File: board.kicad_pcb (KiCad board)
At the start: 2 copper layers, 26.9 x 29 mm, 16 parts, among them J1 PMW3360, J2 MCU, U1 TLV70019_SOT23-5

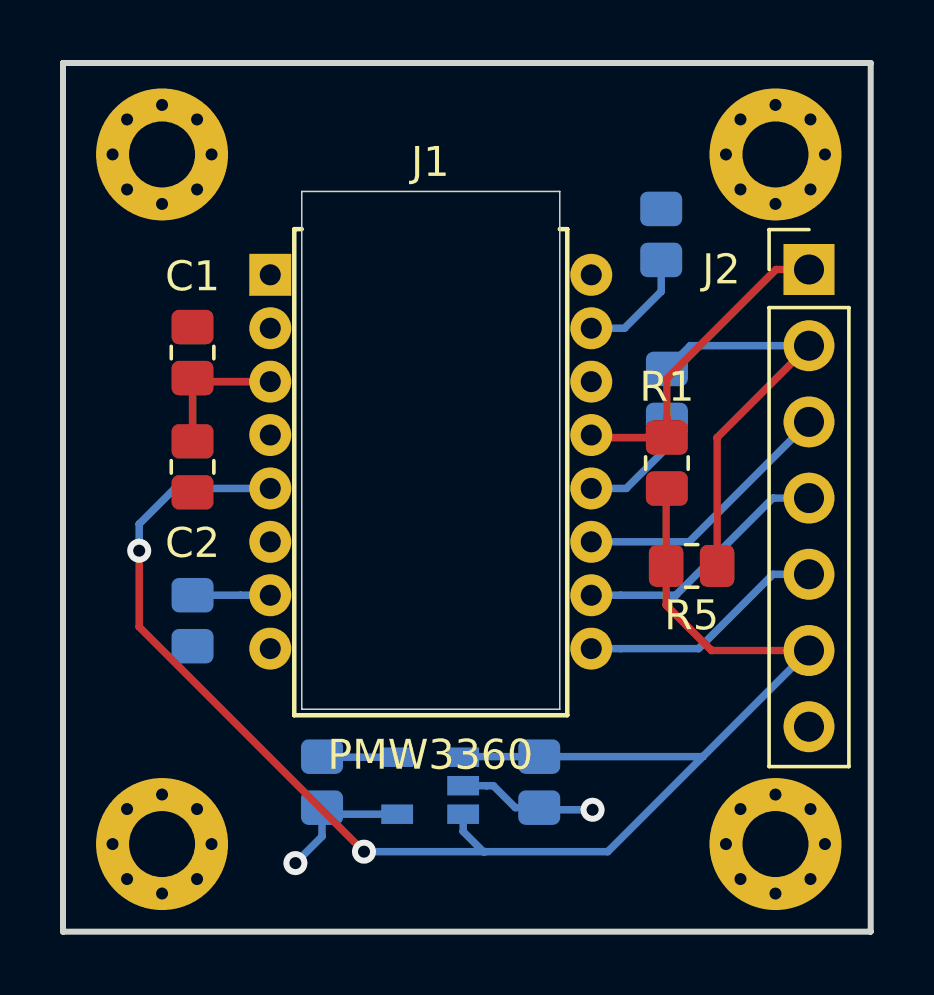
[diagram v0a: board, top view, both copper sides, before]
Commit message: Mounting holes
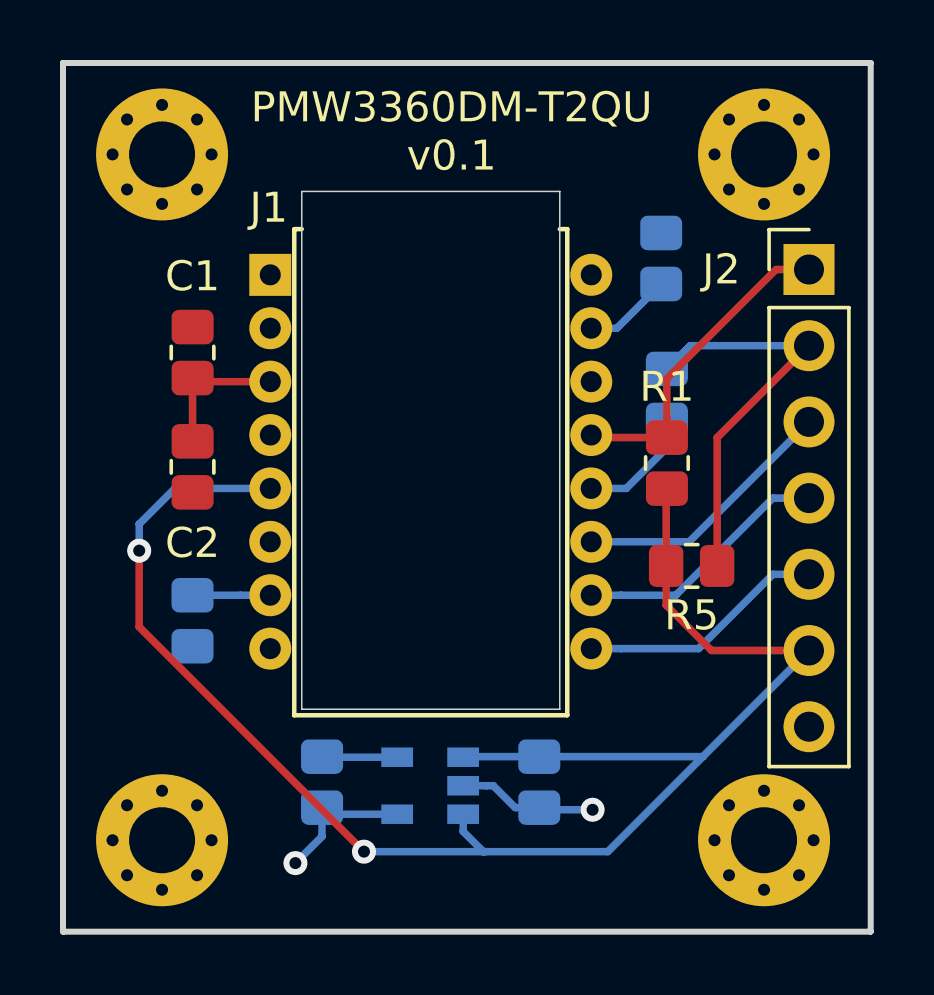
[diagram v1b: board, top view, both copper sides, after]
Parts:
- removed REF** (x4): MountingHole_2.2mm_M2_Pad_Via, MountingHole:MountingHole_2.2mm_M2_Pad_Via
- added J3: Mounting_Hole, MountingHole:MountingHole_2.2mm_M2_Pad_Via, F.Cu at (119.4, 72.4)
- added J4: Mounting_Hole, MountingHole:MountingHole_2.2mm_M2_Pad_Via, F.Cu at (119.4, 49.5)
- added J5: Mounting_Hole, MountingHole:MountingHole_2.2mm_M2_Pad_Via, F.Cu at (139.4, 72.4)
- added J6: Mounting_Hole, MountingHole:MountingHole_2.2mm_M2_Pad_Via, F.Cu at (139.4, 49.5)
- moved R2 0.80 mm to (136.0, 53.0)
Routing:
- net /LED_P: track 3.89 -> 2.94 mm
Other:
- board text added: "PMW3360DM-T2QU v0.1"

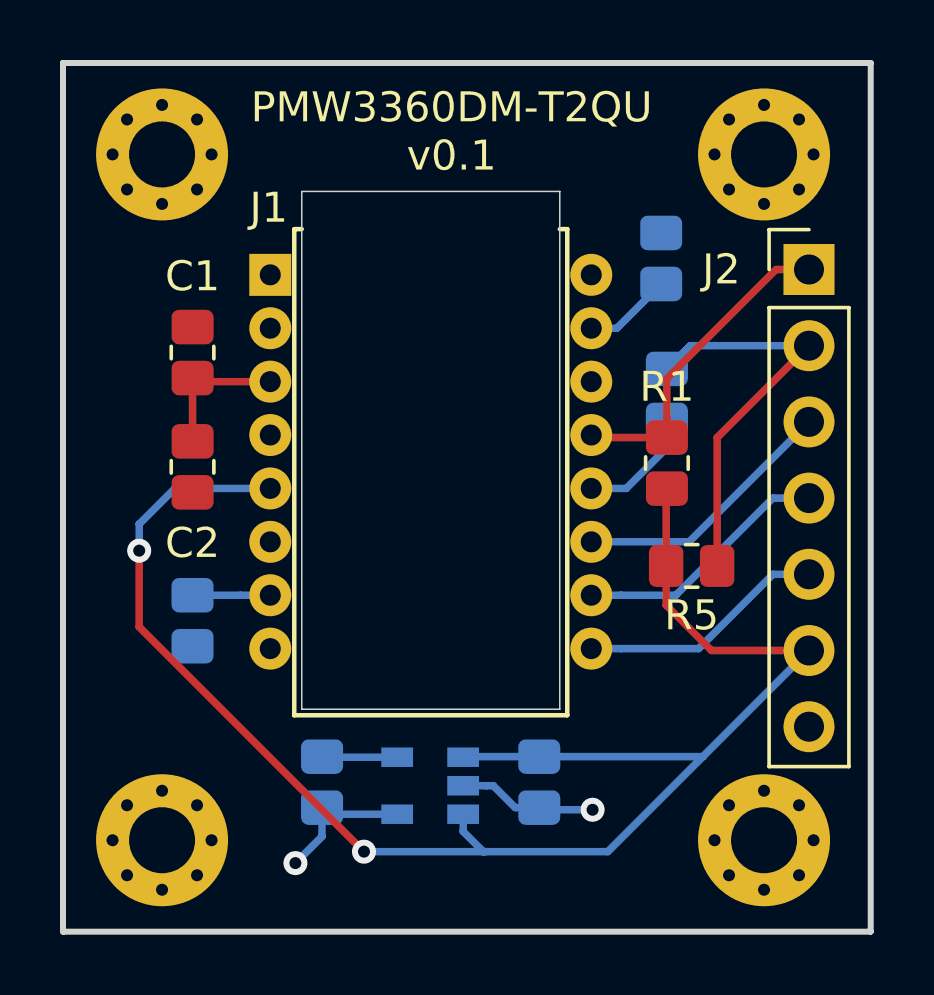
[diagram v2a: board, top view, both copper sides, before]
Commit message: Describe header pins on silkscreen
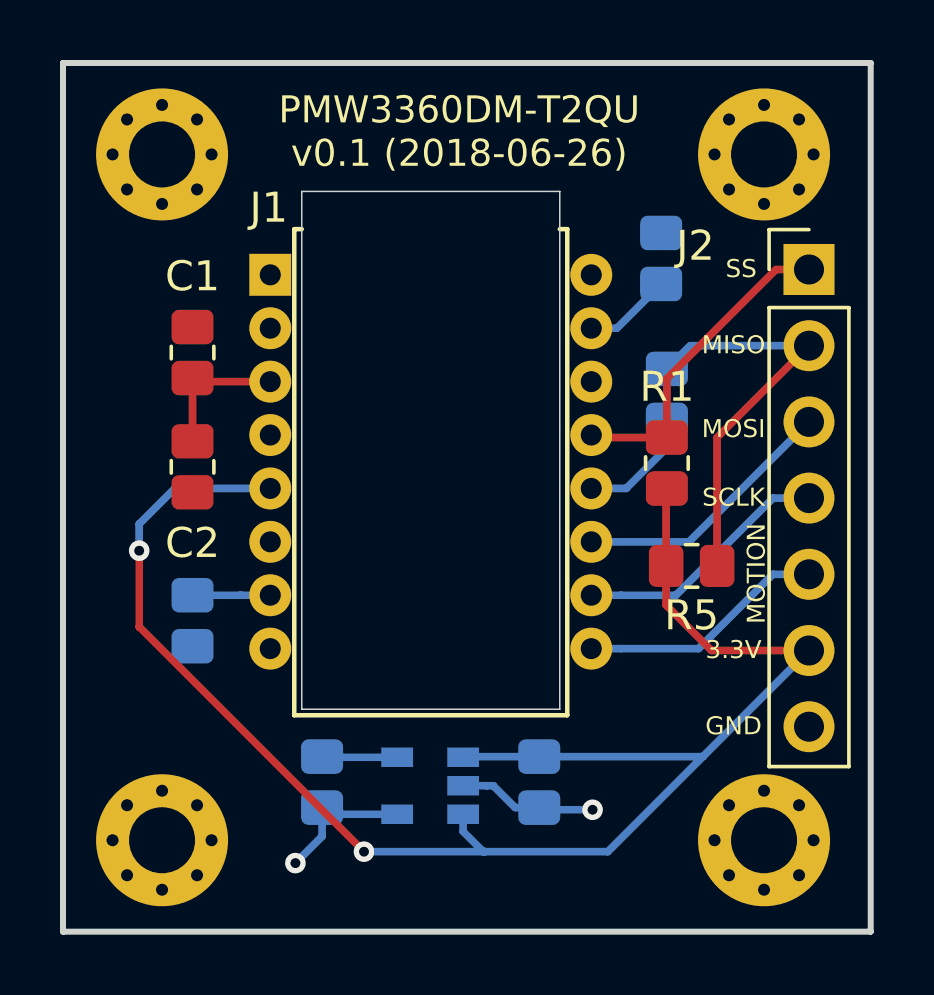
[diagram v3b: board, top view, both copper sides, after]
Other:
- net class Default: clearance 0.25 -> 0.254; trace_width 0.25 -> 0.254; via_dia 0.8 -> 0.6858; via_drill 0.4 -> 0.3302
- rule trace_clearance: 0.25 -> 0.254
- rule trace_min: 0.2 -> 0.1524
- rule via_min_drill: 0.3 -> 0.3302
- rule via_min_size: 0.4 -> 0.6858
- board text added: "3.3V"
- board text added: "GND"
- board text added: "MISO"
- board text added: "MOSI"
- board text added: "MOTION"
- board text added: "PMW3360DM-T2QU v0.1 (2018-06-26)"
- board text added: "SCLK"
- board text added: "SS"
- board text removed: "PMW3360DM-T2QU v0.1"
